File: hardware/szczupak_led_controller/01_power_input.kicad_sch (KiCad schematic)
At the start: 0 parts

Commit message: #5 #3 Added first version of power_input schematic with some required libraries
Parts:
- added C10, C8: 10uF, Capacitor_SMD:C_0805_2012Metric, symbol Device:C
- added C11: 470uF, szczupak_led_controller:EEEFK1V331P, symbol Device:C_Polarized
- added C12, C13, C9: 100nF, Capacitor_SMD:C_0603_1608Metric, symbol Device:C
- added C6, C7: 1uF, Capacitor_SMD:C_0805_2012Metric, symbol Device:C
- added D10: 12V LED, LED_SMD:LED_0805_2012Metric, symbol Device:LED
- added D3: 3V3 LED, LED_SMD:LED_0805_2012Metric, symbol Device:LED
- added D4, D5: D_Zener, Diode_SMD:D_SOD-123F, symbol Device:D_Zener
- added D6, D9: STPS140Z, szczupak_led_controller:SOD3816X145N, symbol Device:D_Schottky
- added D7: SMAJ5.0A-E3_61, szczupak_led_controller:DIOM5127X229N, symbol Diode:PTVS5V0Z1USK
- added D8: SMBJ18A, Diode_SMD:D_SMB, symbol Diode:PTVS5V0Z1USK
- added F1: 0ZCK0050FF2E, szczupak_led_controller:FUSC2214X125N, symbol szczupak_led_controller:0ZCK0050FF2E
- added IC3: TLV75533PDBVR, szczupak_led_controller:SOT95P280X145-5N, symbol szczupak_led_controller:TLV75533PDBVR
- added J4: 43650-0200, 43650-02(00,01,02), symbol szczupak_led_controller:43650-0200
- added J5: 43650-0300, szczupak_led_controller:436500300, symbol szczupak_led_controller:43650-0300
- added Q1: AO4407A, szczupak_led_controller:SOIC127P600X175-8N, symbol szczupak_led_controller:AO4407A
- added Q2: AO3401A, szczupak_led_controller:SOT95P280X125-3N, symbol szczupak_led_controller:AO3401A
- added R10, R12, R9: 100k, Resistor_SMD:R_0603_1608Metric, symbol Device:R
- added R11, R13: 10k, Resistor_SMD:R_0603_1608Metric, symbol Device:R
- added R5: 1k, Resistor_SMD:R_0603_1608Metric, symbol Device:R
- added U3: 3568, szczupak_led_controller:3568, symbol szczupak_led_controller:3568
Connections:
- new net: D4.2 (A), Q2.1 (G), R10.1
- new net: D3.1 (K), R5.1
- new net: D10.1 (K), R11.1
- new net +3.3V: D3.2 (A)
- new net +3V3: C7.1, C8.1, IC3.5 (OUT)
- new net +VIN_LOGIC: C10.1, C6.1, D6.1 (K), D9.1 (K), IC3.1 (IN), IC3.3 (EN)
- new net 12V_FUSE: Q1.5 (D_1), Q1.6 (D_2), Q1.7 (D_3), Q1.8 (D_4), U3.3, U3.4
- new net 12V_IN: J5.1, U3.1, U3.2
- new net 12V_PROT: C11.1, C12.1, D10.2 (A), D5.1 (K), D8.1 (K), Q1.1 (S_1), Q1.2 (S_2), Q1.3 (S_3), R12.1
- new net 5V_FUSE: F1.2, Q2.3 (D)
- new net 5V_IN: F1.1, J4.1
- new net 5V_PROT: C13.1, D4.1 (K), D7.1 (K), D9.2 (A), Q2.2 (S)
- new net ADC_12V: C9.1, R12.2, R13.1
- new net GND: C10.2, C11.2, C12.2, C13.2, C6.2, C7.2, C8.2, C9.2, D7.2 (A), D8.2 (A), IC3.2 (GND), J4.2, J5.3, R10.2, R11.2, R13.2, R5.2, R9.2
- new net R_gate: D5.2 (A), Q1.4 (G), R9.1
- new net USB_5V: D6.2 (A)
- no-connect marks 0 -> 2
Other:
- note added: "12V ADC"
- note added: "12V POWER INPUT"
- note added: "5V POWER INPUT"
- note added: "LDO"
- note added: "POWER LEDs"
- title: (none) -> led_controller - 03_power_input

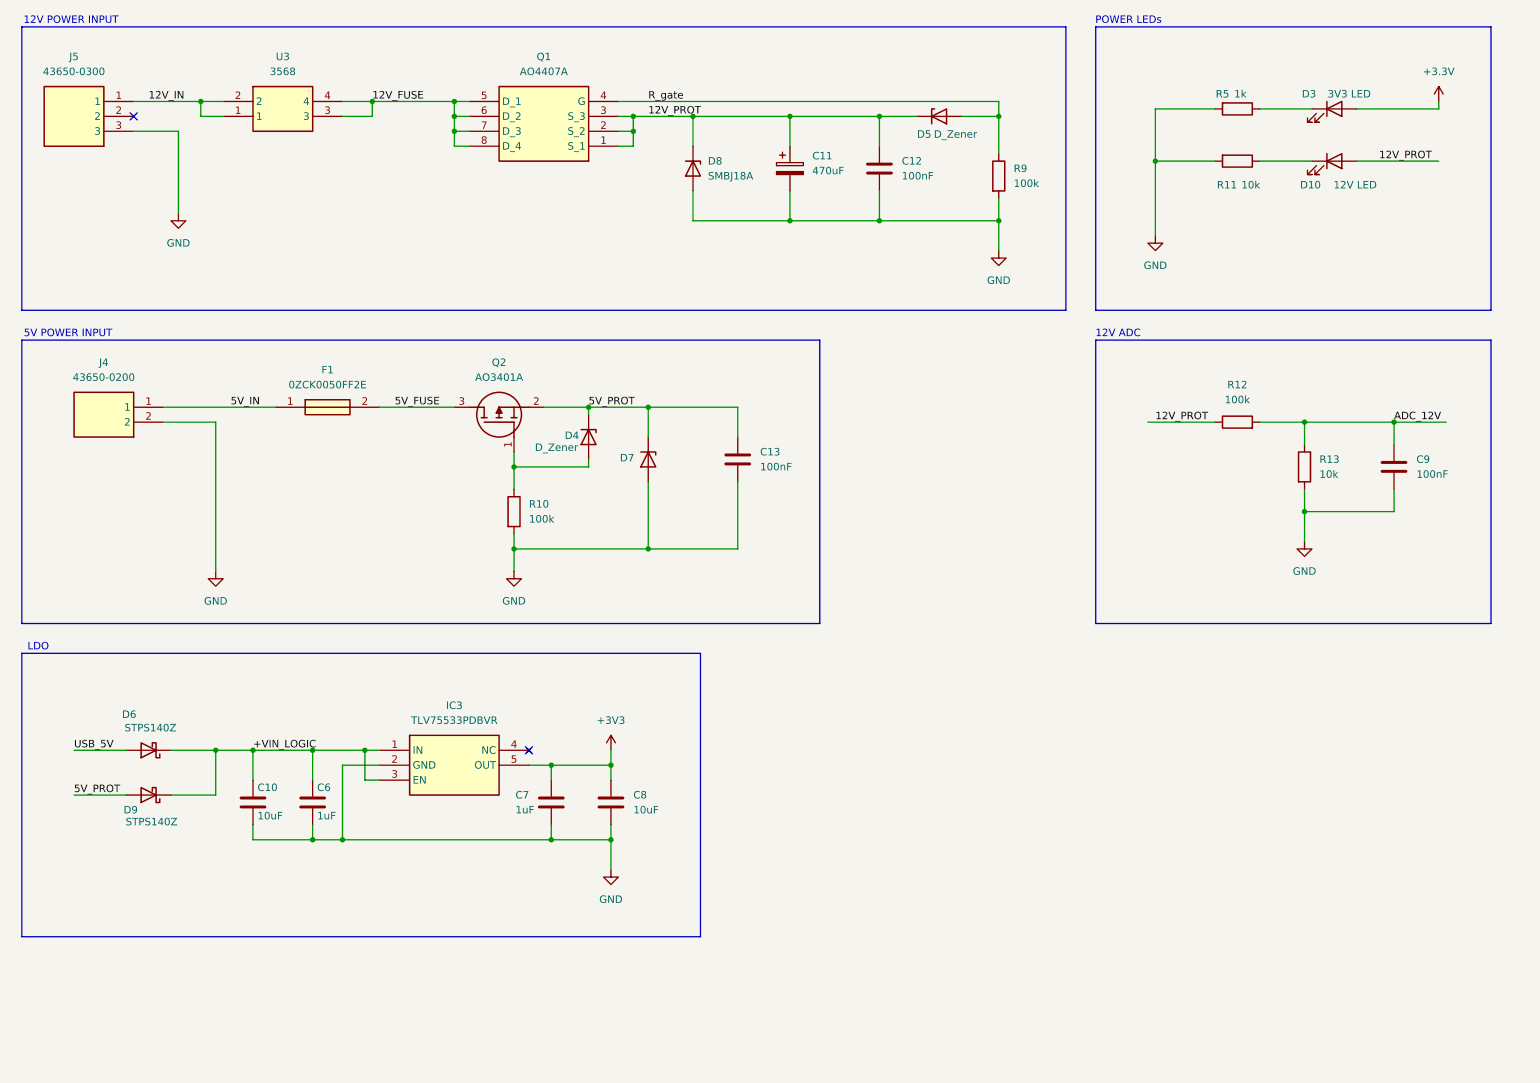
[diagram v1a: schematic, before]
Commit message: #4 #6 Added power output and interfaces schematics
Designed initial placement for most important components on pcb
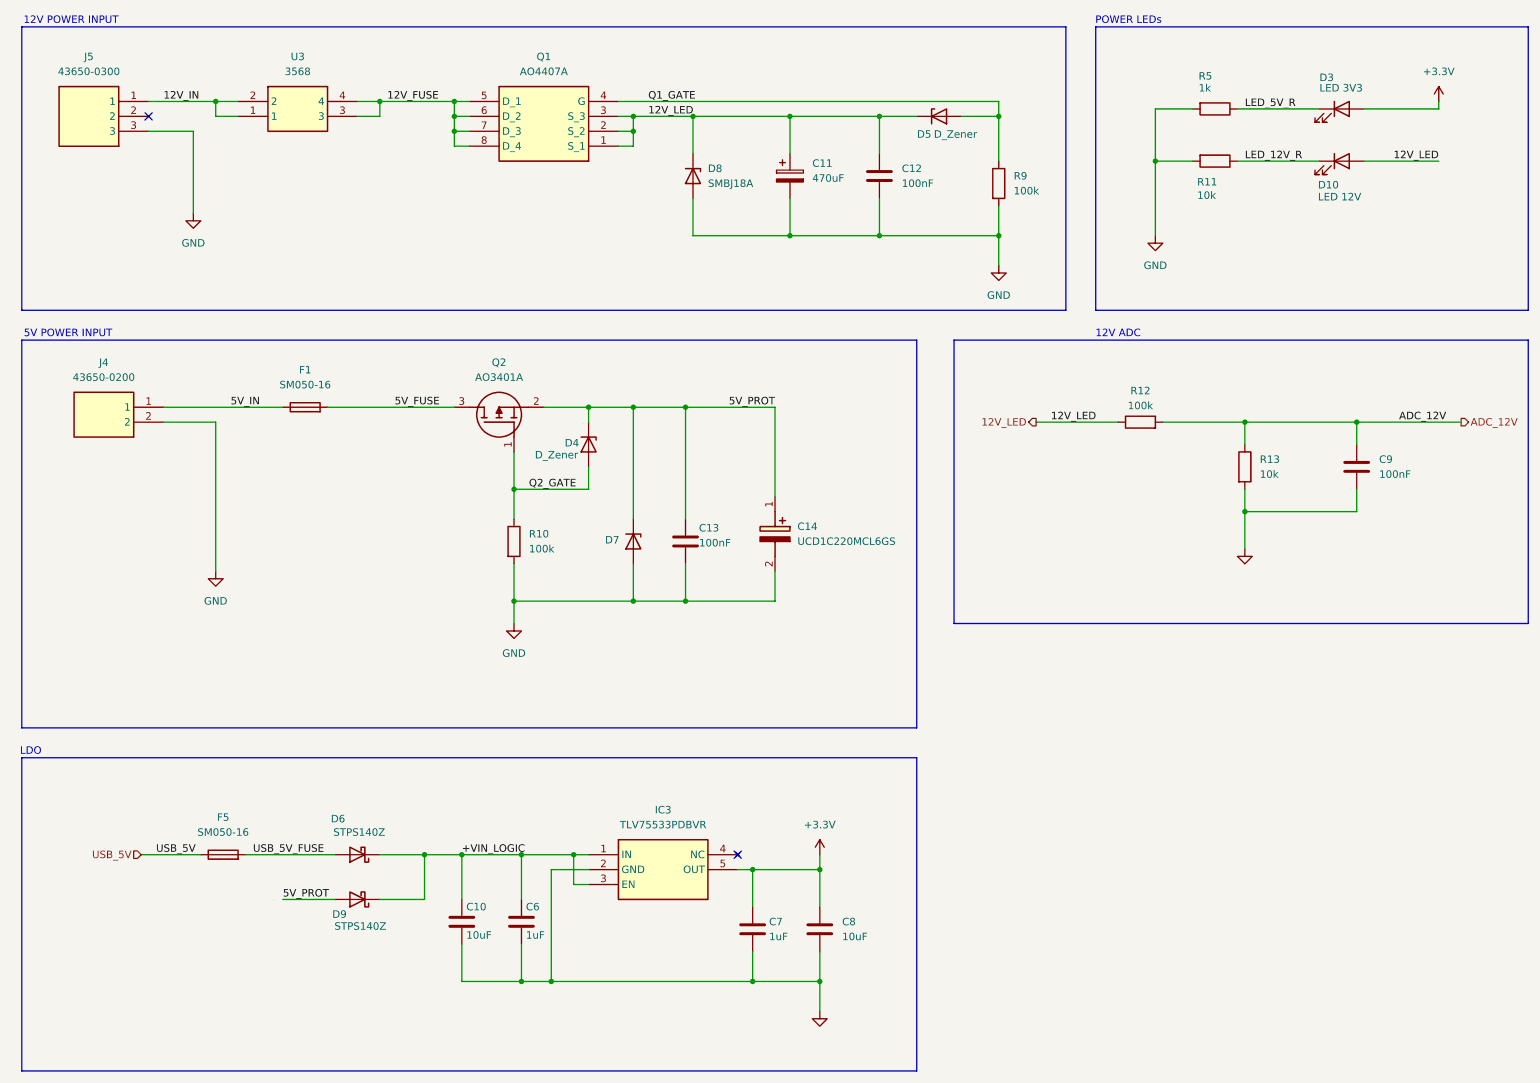
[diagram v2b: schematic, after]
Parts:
- removed F1: 0ZCK0050FF2E, szczupak_led_controller:FUSC2214X125N, symbol szczupak_led_controller:0ZCK0050FF2E
- added C14: UCD1C220MCL6GS, szczupak_led_controller:CAPAE430X610N, symbol szczupak_led_controller:UCD1C220MCL6GS
- added F1, F5: SM050-16, Fuse:Fuse_1210_3225Metric, symbol Device:Fuse
- D10: value 12V LED -> LED 12V
- D3: value 3V3 LED -> LED 3V3
- J4: footprint 43650-02(00,01,02) -> szczupak_led_controller:43650-02_00,01,02_
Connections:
- net +3V3 is gone; now on net +3.3V: C7.1, C8.1, IC3.5 (OUT)
- net 5V_FUSE: now also F1.2
- net 5V_IN: now also F1.1
- net 5V_PROT: now also C14.1 (+)
- net GND: now also C14.2 (-)
- net USB_5V: now also F5.1; no longer D6.2 (A)
- net Q2_GATE: now reaches D4.2 (A), Q2.1 (G), R10.1
- net LED_5V_R: now reaches D3.1 (K), R5.1
- net LED_12V_R: now reaches D10.1 (K), R11.1
- net 12V_PROT renamed 12V_LED
- net R_gate renamed Q1_GATE
- new net USB_5V_FUSE: D6.2 (A), F5.2
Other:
- company: (none) -> AGH Marines
- title: led_controller - 03_power_input -> led_controller - 01_power_input
- moved on the sheet: C10, C11, C12, C13, C6, C7, C8, C9, D10, D3, D4, D6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
